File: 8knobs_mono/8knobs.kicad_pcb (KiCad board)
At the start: 2 copper layers, 31 parts, among them J1 Conn_01x04_Female, U1 PC900, U2 BluePill_STM32F103C

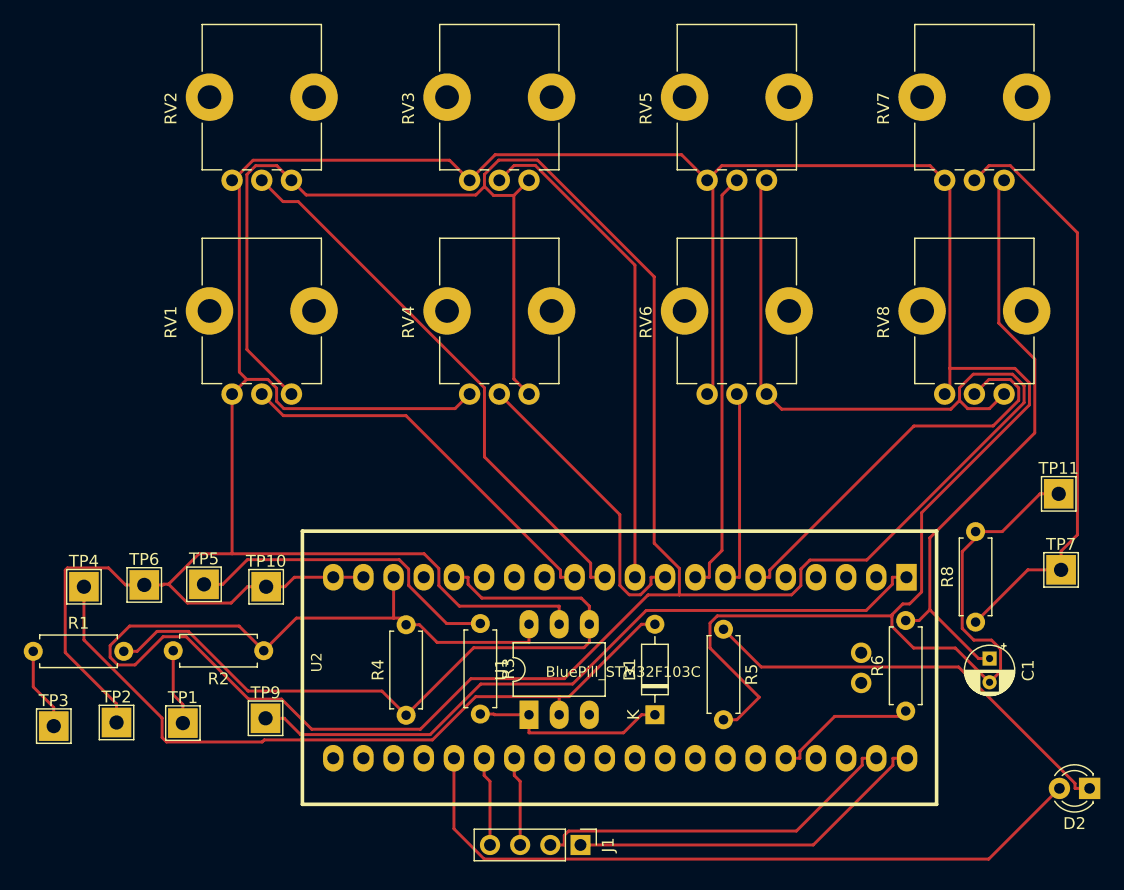
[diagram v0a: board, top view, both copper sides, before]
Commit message: v1.1 of 8knobs mono:  - corrected wrong connection to battery  - easier PCB manufacturing
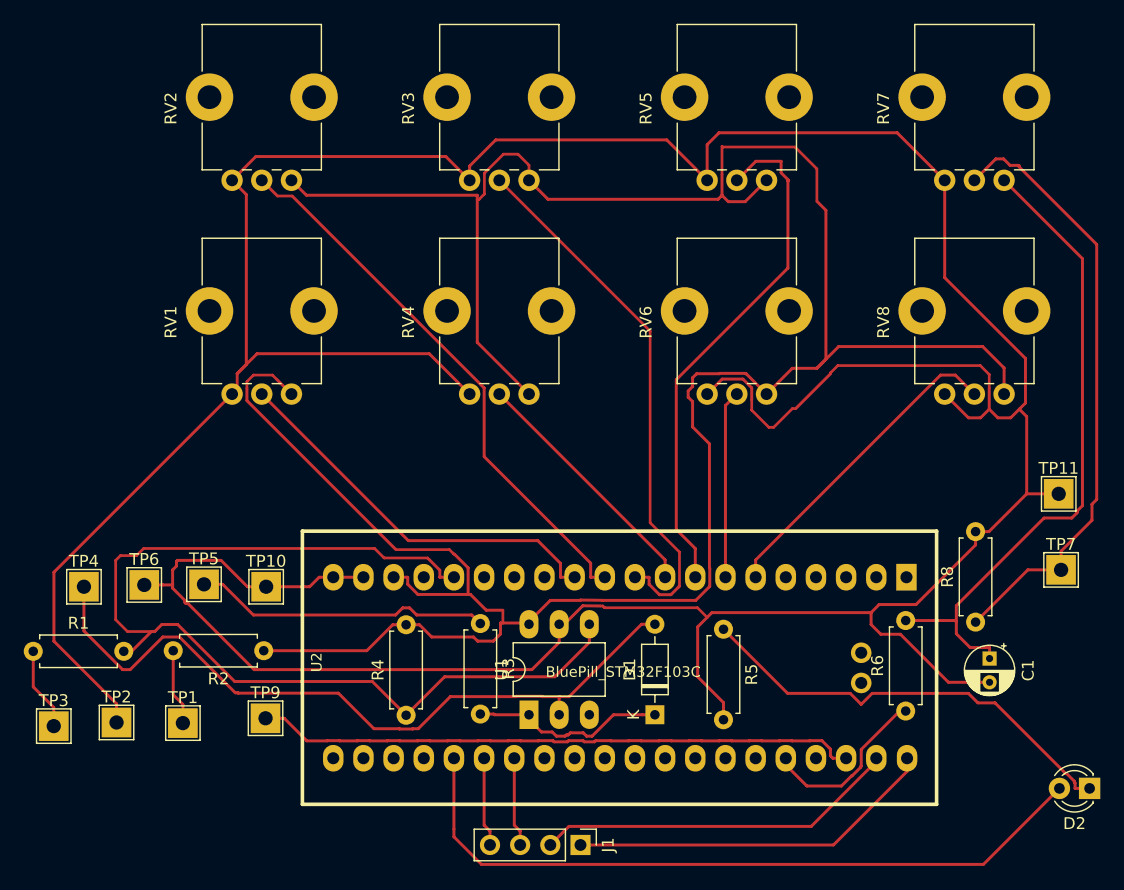
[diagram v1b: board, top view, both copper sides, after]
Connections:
- U2 pad 1: Net-(TP9-Pad1) -> (no net)
- U2 pad 38: (no net) -> Net-(TP9-Pad1)
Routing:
- net +3V3: track 298.6 -> 232.0 mm
- net Net-(R1-Pad2): track 61.2 -> 86.2 mm
- net GND: track 329.2 -> 348.0 mm
- net Net-(TP9-Pad1): track 60.4 -> 51.0 mm
- net Net-(RV5-Pad2): track 35.6 -> 44.3 mm
- net Net-(RV8-Pad2): track 34.3 -> 27.0 mm
- net Net-(C1-Pad1): track 50.4 -> 55.2 mm
- net Net-(RV4-Pad2): track 25.4 -> 21.2 mm
- net Net-(RV3-Pad2): track 41.7 -> 45.6 mm
- net Net-(R6-Pad1): track 12.1 -> 14.9 mm
- net Net-(R8-Pad1): track 49.5 -> 51.8 mm
- net Net-(R3-Pad1): track 27.2 -> 25.1 mm
- net Net-(RV6-Pad2): track 16.7 -> 15.8 mm
- net Net-(D2-Pad1): track 36.6 -> 37.5 mm
- net Net-(D2-Pad2): track 60.4 -> 61.2 mm
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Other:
- net class Default: clearance 0.2 -> 0.23; trace_width 0.25 -> 0.23
- rule trace_clearance: 0.2 -> 0.23
